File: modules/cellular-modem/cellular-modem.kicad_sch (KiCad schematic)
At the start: 1 part, among them J1 Bus_PCI_Express_Mini

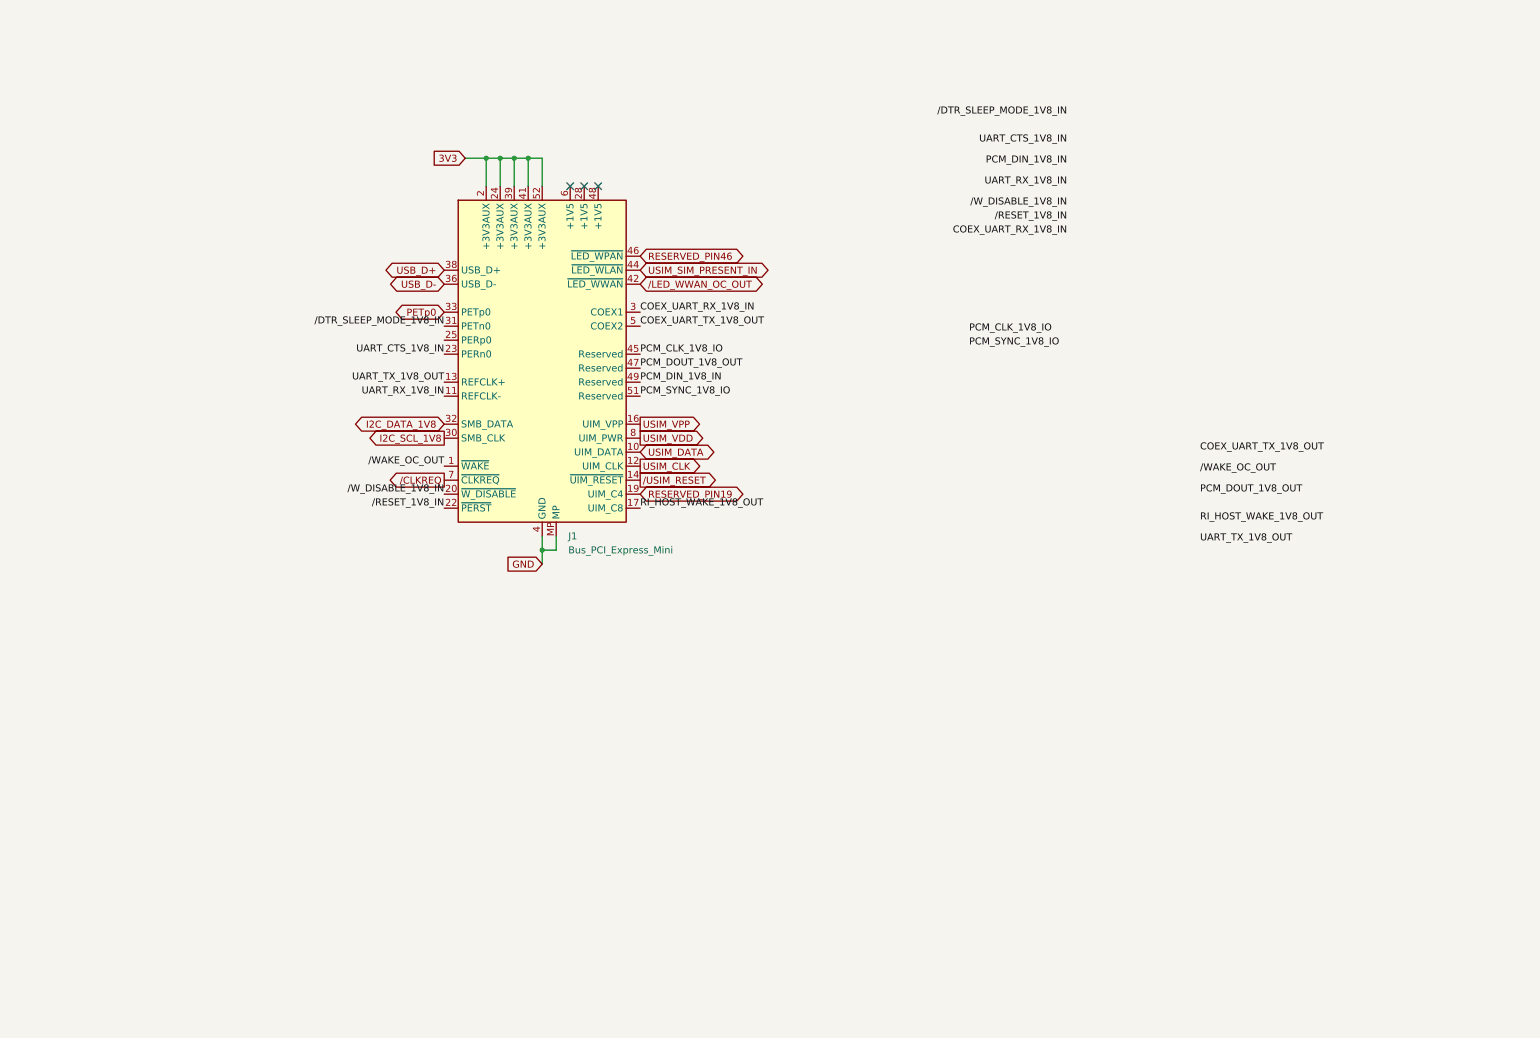
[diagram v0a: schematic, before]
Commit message: more work on cellular modem module
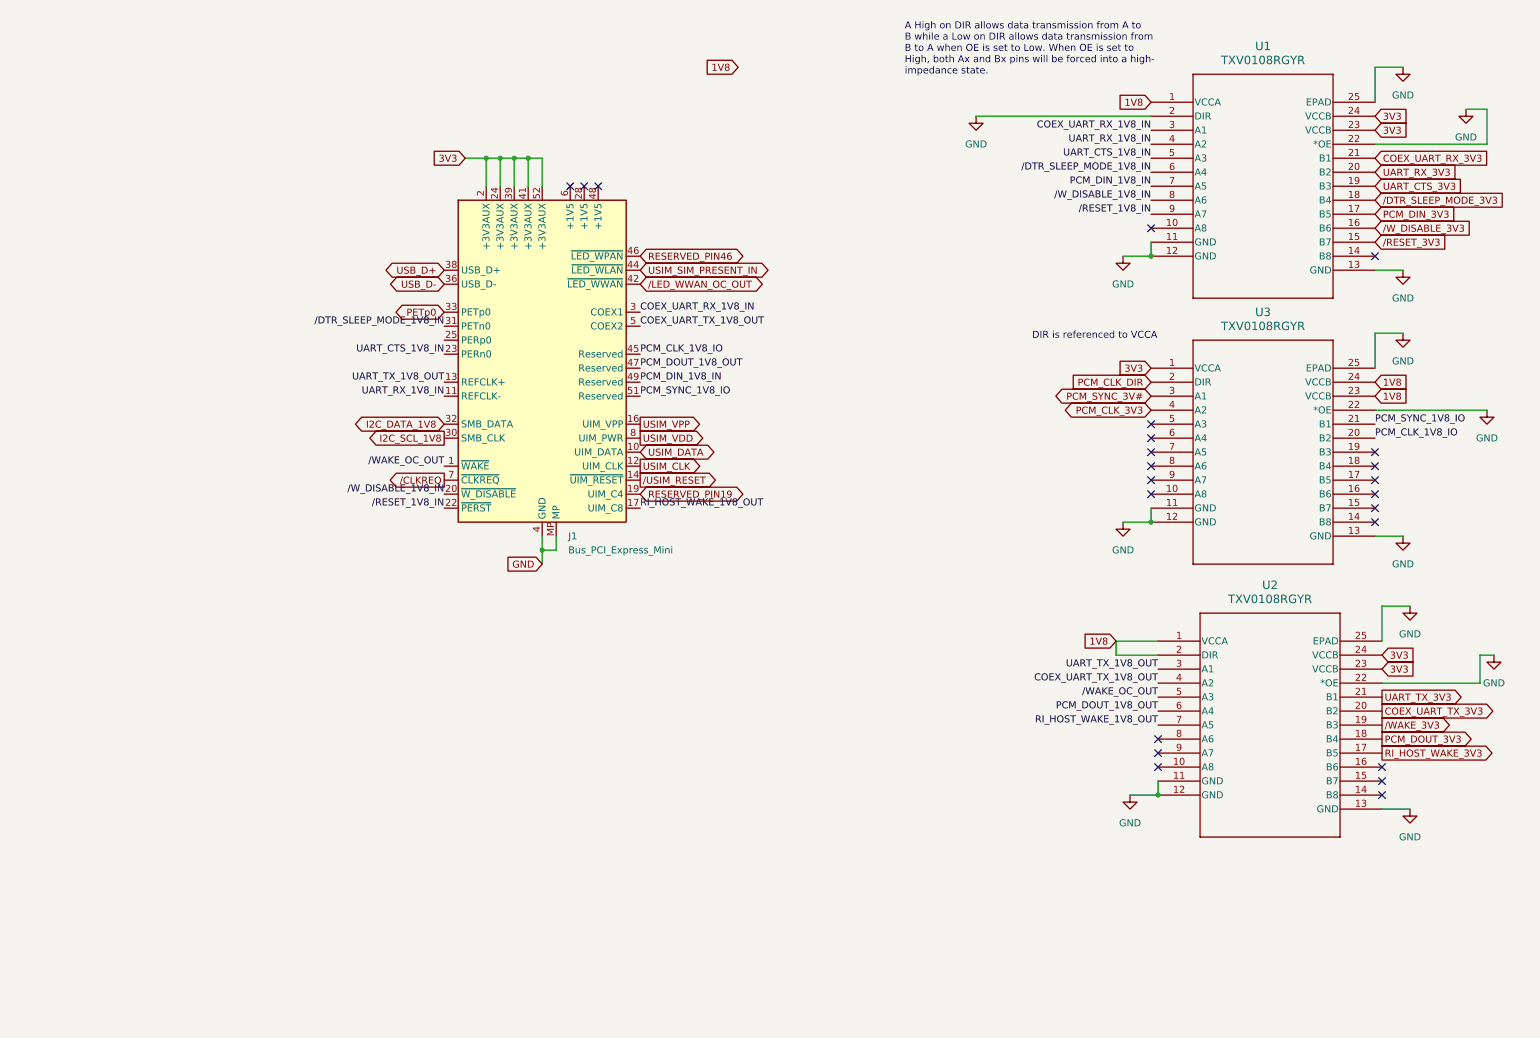
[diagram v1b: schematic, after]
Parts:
- added U1, U2, U3: TXV0108RGYR, VQFN24_RGY_TEX, symbol 2025-02-22_10-37-39:TXV0108RGYR
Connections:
- net 3V3: now also U1.23 (VCCB), U1.24 (VCCB), U2.23 (VCCB), U2.24 (VCCB), U3.1 (VCCA)
- net COEX_UART_RX_1V8_IN: now also U1.3 (A1)
- net COEX_UART_TX_1V8_OUT: now also U2.4 (A2)
- net GND: now also U1.11 (GND), U1.12 (GND), U1.13 (GND), U1.2 (DIR), U1.22 (*OE), U1.25 (EPAD), U2.11 (GND), U2.12 (GND), U2.13 (GND), U2.22 (*OE), U2.25 (EPAD), U3.11 (GND), U3.12 (GND), U3.13 (GND), U3.22 (*OE), U3.25 (EPAD)
- net PCM_CLK_1V8_IO: now also U3.20 (B2)
- net PCM_DIN_1V8_IN: now also U1.7 (A5)
- net PCM_DOUT_1V8_OUT: now also U2.6 (A4)
- net PCM_SYNC_1V8_IO: now also U3.21 (B1)
- net RI_HOST_WAKE_1V8_OUT: now also U2.7 (A5)
- net UART_CTS_1V8_IN: now also U1.5 (A3)
- net UART_RX_1V8_IN: now also U1.4 (A2)
- net UART_TX_1V8_OUT: now also U2.3 (A1)
- net /DTR_SLEEP_MODE_1V8_IN: now also U1.6 (A4)
- net /RESET_1V8_IN: now also U1.9 (A7)
- net /WAKE_OC_OUT: now also U2.5 (A3)
- net /W_DISABLE_1V8_IN: now also U1.8 (A6)
- new net 1V8: U1.1 (VCCA), U2.1 (VCCA), U2.2 (DIR), U3.23 (VCCB), U3.24 (VCCB)
- new net COEX_UART_RX_3V3: U1.21 (B1)
- new net COEX_UART_TX_3V3: U2.20 (B2)
- new net PCM_CLK_3V3: U3.4 (A2)
- new net PCM_CLK_DIR: U3.2 (DIR)
- new net PCM_DIN_3V3: U1.17 (B5)
- new net PCM_DOUT_3V3: U2.18 (B4)
- new net PCM_SYNC_3V#: U3.3 (A1)
- new net RI_HOST_WAKE_3V3: U2.17 (B5)
- new net UART_CTS_3V3: U1.19 (B3)
- new net UART_RX_3V3: U1.20 (B2)
- new net UART_TX_3V3: U2.21 (B1)
- new net /DTR_SLEEP_MODE_3V3: U1.18 (B4)
- new net /RESET_3V3: U1.15 (B7)
- new net /WAKE_3V3: U2.19 (B3)
- new net /W_DISABLE_3V3: U1.16 (B6)
- no-connect marks 3 -> 23
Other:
- note added: "A High on DIR allows data transmission from A to B while a Low on DIR allows data transmission from B to A when OE is set to Low. When OE is set to High, both Ax and Bx pins will be forced into a high- impedance state."
- note added: "DIR is referenced to VCCA"

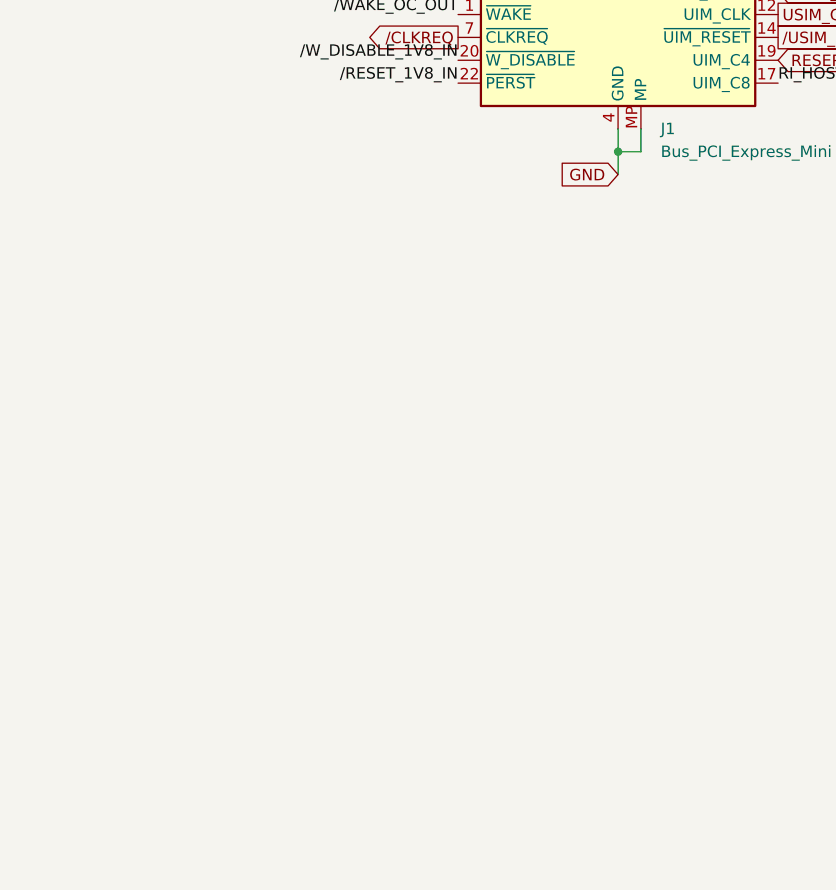
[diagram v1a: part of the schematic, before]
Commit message: layout USB lines to alegedly have correct impedance
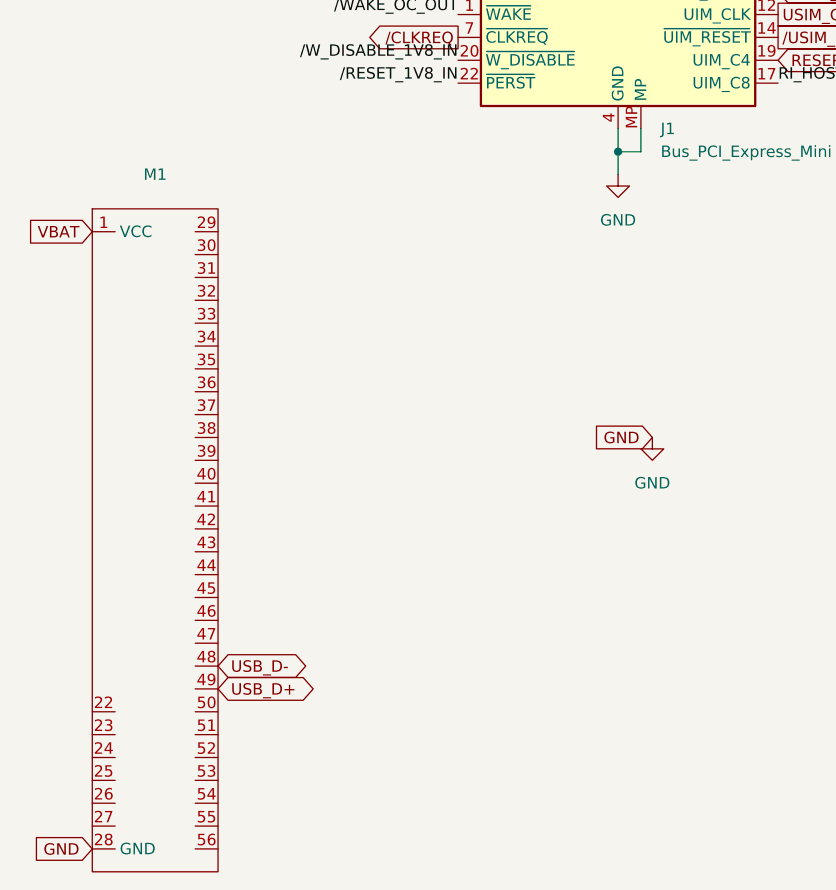
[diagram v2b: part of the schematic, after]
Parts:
- added M1: ~, MegaCastle:MegaCastle2x28-Module-I36.0x66.3-M800007FFFFFFFF-NIBBLE, symbol MegaCastle:MegaCastle2x28-Module-I36.0x66.3-M800007FFFFFFFF-NOCUTOUT
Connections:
- net GND: now also M1.28 (GND)
- net USB_D+: now also M1.49
- net USB_D-: now also M1.48
- new net VBAT: M1.1 (VCC)

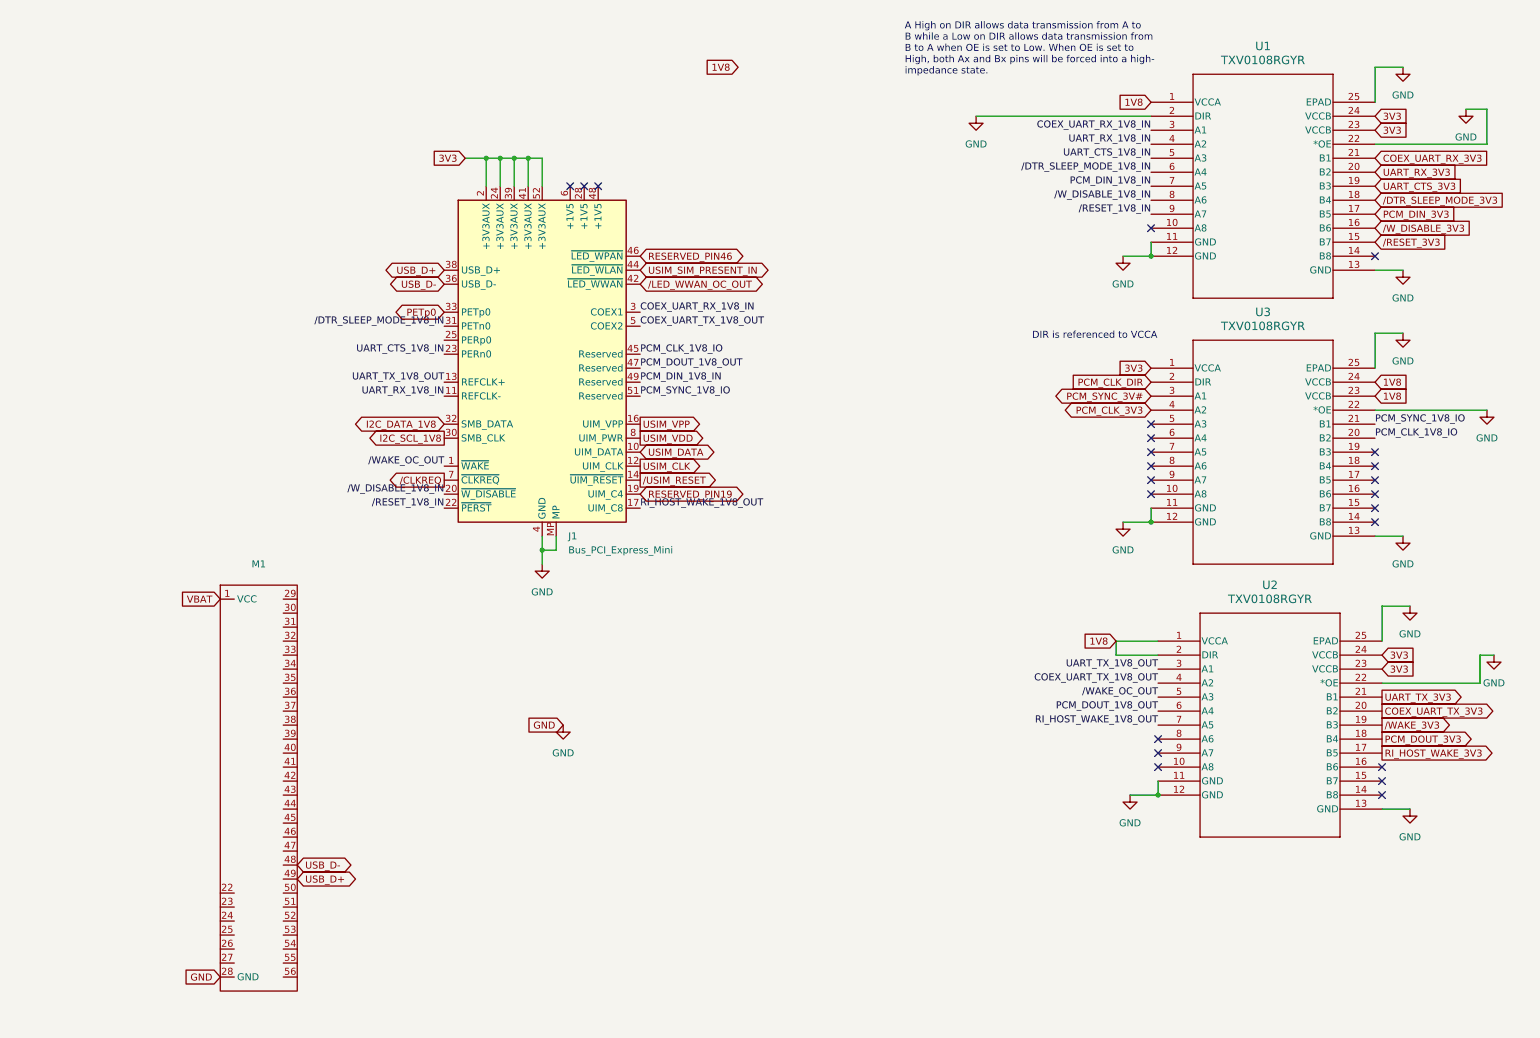
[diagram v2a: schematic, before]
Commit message: add 3.3V and 1.8V DC:DC to cellular modem module
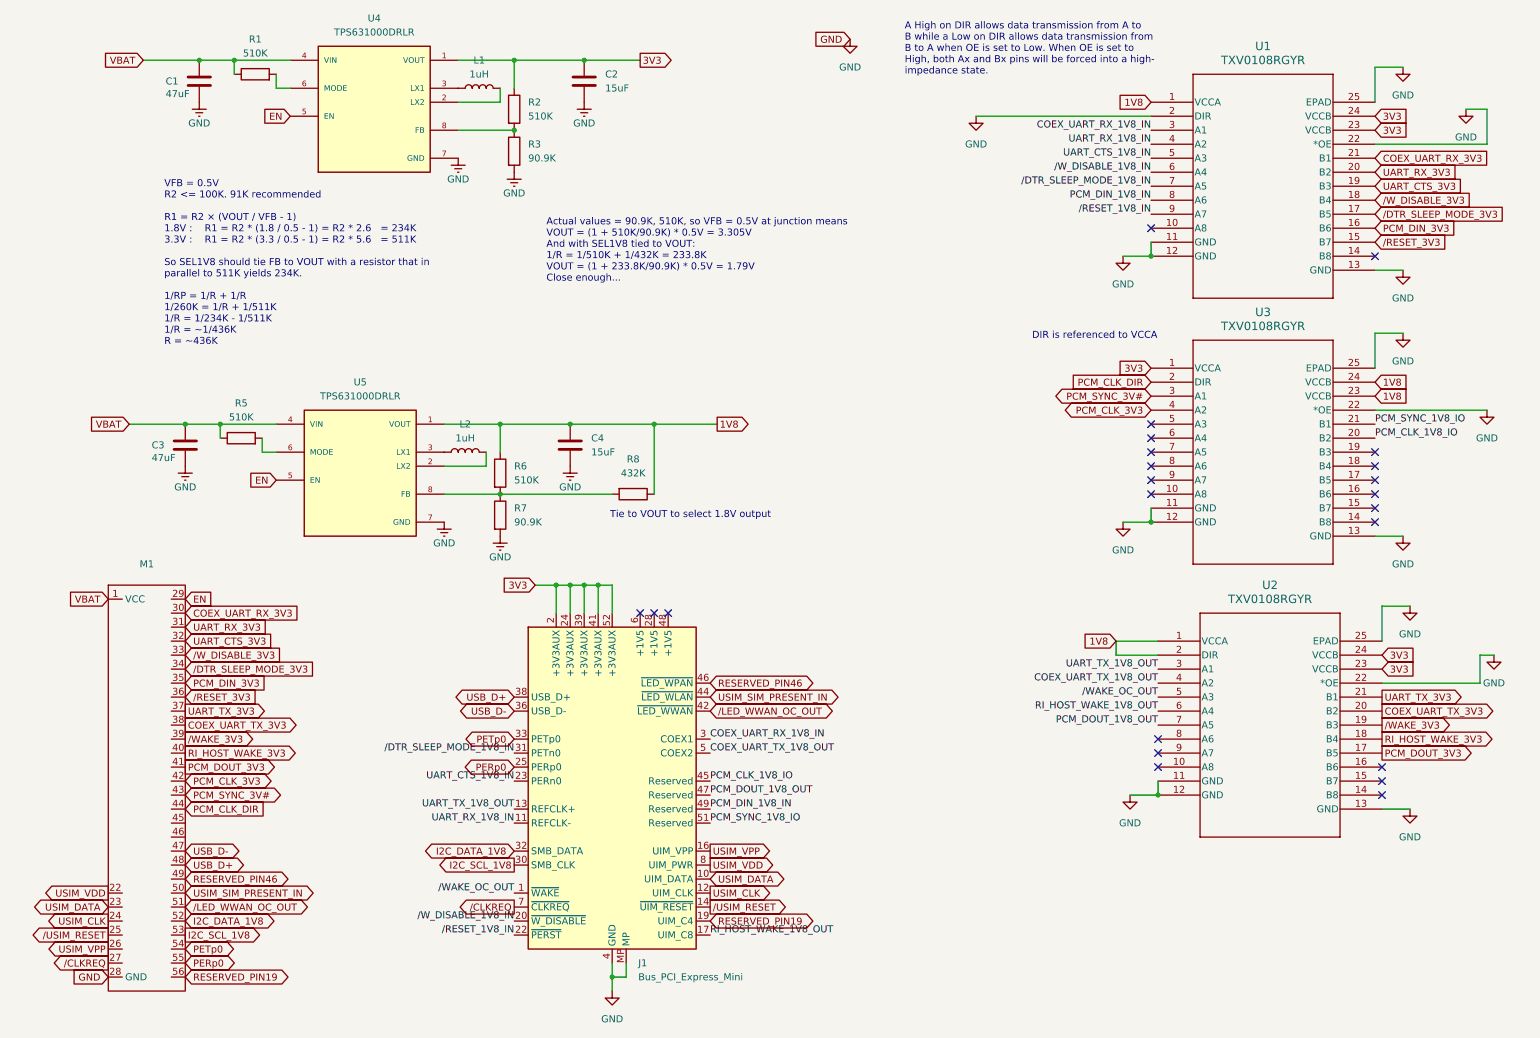
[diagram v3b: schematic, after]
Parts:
- added C1, C3: 47uF, Capacitor_SMD:C_0805_2012Metric, symbol Device:C
- added C2, C4: 15uF, Capacitor_SMD:C_0805_2012Metric, symbol Device:C
- added L1, L2: 1uH, Inductor_SMD:L_1008_2520Metric_Pad1.43x2.20mm_HandSolder, symbol Device:L
- added R1, R2, R5, R6: 510K, Resistor_SMD:R_0805_2012Metric, symbol Device:R
- added R3, R7: 90.9K, Resistor_SMD:R_0805_2012Metric, symbol Device:R
- added R8: 432K, Resistor_SMD:R_0805_2012Metric, symbol Device:R
- added U4, U5: TPS631000DRLR, SOT50P160X60-8N, symbol TPS631000DRLR:TPS631000DRLR
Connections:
- net 1V8: now also C4.1, R6.1, R8.1, U5.1 (VOUT)
- net 3V3: now also C2.1, R2.1, U4.1 (VOUT)
- net COEX_UART_RX_3V3: now also M1.30
- net COEX_UART_TX_3V3: now also M1.38
- net GND: now also C1.1, C2.2, C3.1, C4.2, R3.2, R7.2, U4.7 (GND), U5.7 (GND)
- net I2C_DATA_1V8: now also M1.52
- net I2C_SCL_1V8: now also M1.53
- net PCM_CLK_3V3: now also M1.42
- net PCM_CLK_DIR: now also M1.44
- net PCM_DIN_1V8_IN: now also U1.8 (A6); no longer U1.7 (A5)
- net PCM_DIN_3V3: now also M1.35, U1.16 (B6); no longer U1.17 (B5)
- net PCM_DOUT_1V8_OUT: now also U2.7 (A5); no longer U2.6 (A4)
- net PCM_DOUT_3V3: now also M1.41, U2.17 (B5); no longer U2.18 (B4)
- net PCM_SYNC_3V#: now also M1.43
- net PETp0: now also M1.54
- net RESERVED_PIN19: now also M1.56
- net RESERVED_PIN46: now also M1.49
- net RI_HOST_WAKE_1V8_OUT: now also U2.6 (A4); no longer U2.7 (A5)
- net RI_HOST_WAKE_3V3: now also M1.40, U2.18 (B4); no longer U2.17 (B5)
- net UART_CTS_3V3: now also M1.32
- net UART_RX_3V3: now also M1.31
- net UART_TX_3V3: now also M1.37
- net USB_D+: now also M1.48; no longer M1.49
- net USB_D-: now also M1.47; no longer M1.48
- net USIM_CLK: now also M1.24
- net USIM_DATA: now also M1.23
- net USIM_SIM_PRESENT_IN: now also M1.50
- net USIM_VDD: now also M1.22
- net USIM_VPP: now also M1.26
- net VBAT: now also C1.2, C3.2, R1.1, R5.1, U4.4 (VIN), U5.4 (VIN)
- net /CLKREQ: now also M1.27
- net /DTR_SLEEP_MODE_1V8_IN: now also U1.7 (A5); no longer U1.6 (A4)
- net /DTR_SLEEP_MODE_3V3: now also M1.34, U1.17 (B5); no longer U1.18 (B4)
- net /LED_WWAN_OC_OUT: now also M1.51
- net /RESET_3V3: now also M1.36
- net /USIM_RESET: now also M1.25
- net /WAKE_3V3: now also M1.39
- net /W_DISABLE_1V8_IN: now also U1.6 (A4); no longer U1.8 (A6)
- net /W_DISABLE_3V3: now also M1.33, U1.18 (B4); no longer U1.16 (B6)
- net EN: now reaches M1.29
- net EN: now also U4.5 (EN), U5.5 (EN)
- net PERp0: now reaches M1.55
- net PERp0: now also J1.25 (PERp0)
- new net: L1.1, U4.3 (LX1)
- new net: L1.2, U4.2 (LX2)
- new net: R1.2, U4.6 (MODE)
- new net: R2.2, R3.1, U4.8 (FB)
- new net: R6.2, R7.1, R8.2, U5.8 (FB)
- new net: L2.2, U5.2 (LX2)
- new net: L2.1, U5.3 (LX1)
- new net: R5.2, U5.6 (MODE)
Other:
- note added: "Actual values = 90.9K, 510K, so VFB = 0.5V at junction means VOUT = (1 + 510K/90.9K) * 0.5V = 3.305V And with SEL1V8 tied to VOUT: 1/R = 1/510K + 1/432K = 233.8K VOUT = (1 + 233.8K/90.9K) * 0.5V = 1.79V Close enough..."
- note added: "Tie to VOUT to select 1.8V output"
- note added: "VFB = 0.5V R2 <= 100K. 91K recommended R1 = R2 × (VOUT / VFB - 1) 1.8V : R1 = R2 * (1.8 / 0.5 - 1) = R2 * 2.6 = 234K 3.3V : R1 = R2 * (3.3 / 0.5 - 1) = R2 * 5.6 = 511K So SEL1V8 should tie FB to VOUT with a resistor that in parallel to 511K yields 234K. 1/RP = 1/R + 1/R 1/260K = 1/R + 1/511K 1/R = 1/234K - 1/511K 1/R = ~1/436K R = ~436K"
- moved on the sheet: J1, M1
